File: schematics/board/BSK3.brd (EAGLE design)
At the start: 82 x 100 mm, 44 parts

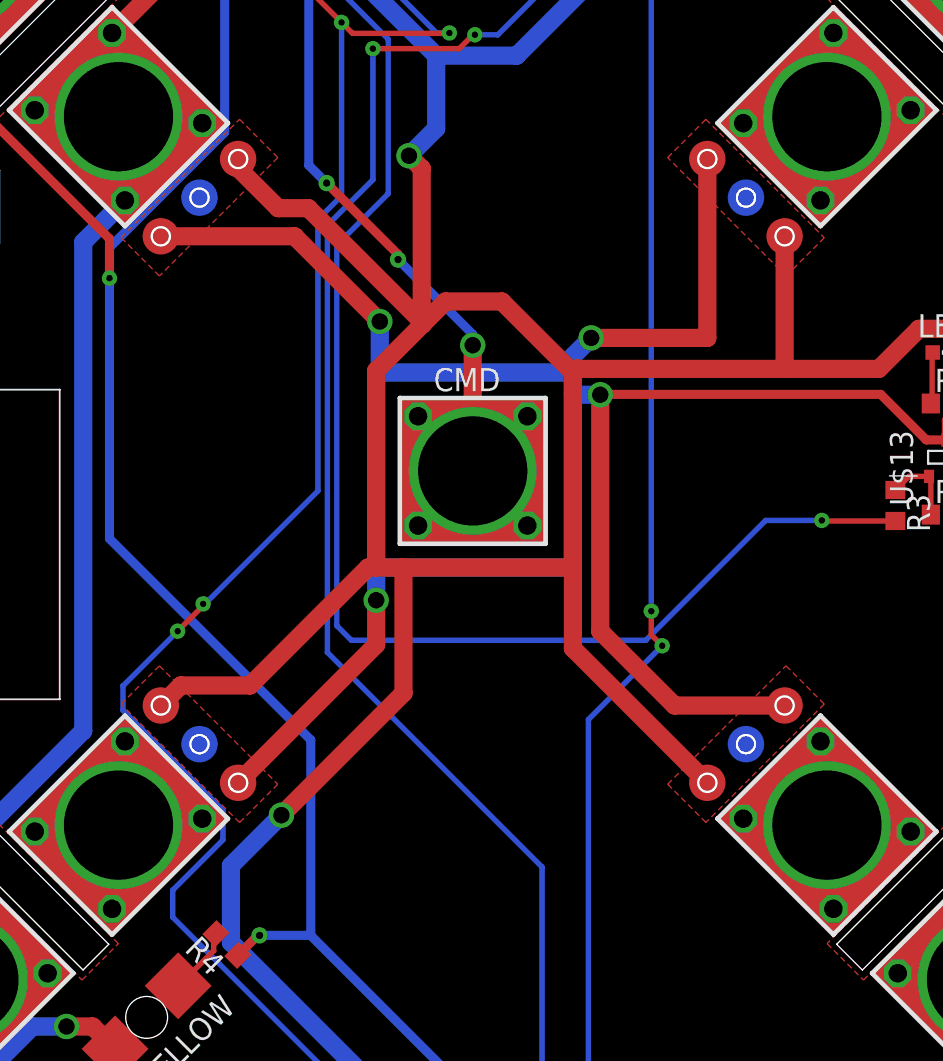
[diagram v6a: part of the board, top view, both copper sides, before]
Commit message: Изменены площадки для сплавов Розе
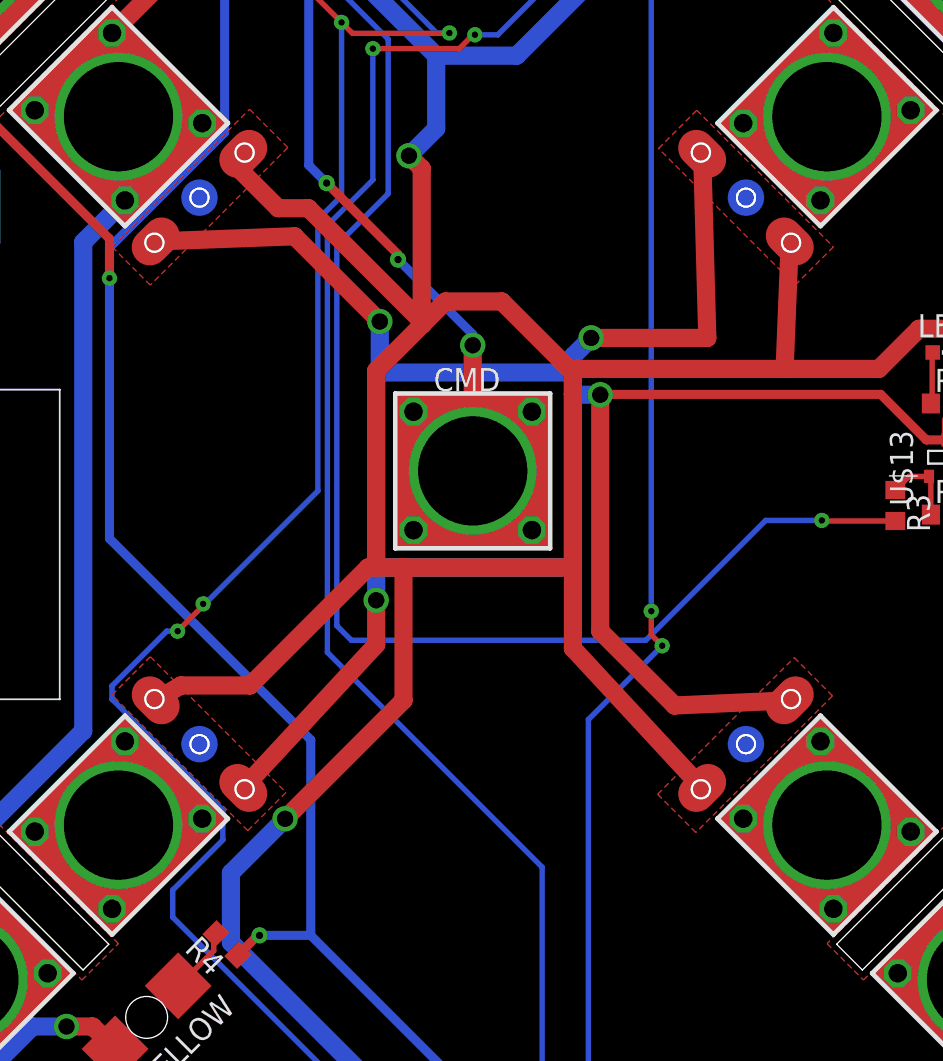
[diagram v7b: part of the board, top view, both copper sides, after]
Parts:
- U$15, U$16, U$6, U$7: value GRAFITGRAFIT3_1 -> GRAFITGRAFIT4_2; device CanCubeSat:GRAFIT3_1 -> CanCubeSat:GRAFIT4_2
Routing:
- net B3-CMD: track 77.6 -> 79.0 mm
- net 2: track 142.1 -> 142.9 mm
- net 1W: track 126.7 -> 127.5 mm
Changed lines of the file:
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@@
 <attribute name="VALUE" x="66.365" y="45.695" size="1.27" layer="27"/>
 </element>
-<element name="U$6" library="CanCubeSat" package="GRAFIT3_1" value="GRAFITGRAFIT3_1" x="26" y="65" smashed="yes" rot="R135"/>
-<element name="U$7" library="CanCubeSat" package="GRAFIT3_1" value="GRAFITGRAFIT3_1" x="26" y="35" smashed="yes" rot="R225"/>
-<element name="U$15" library="CanCubeSat" package="GRAFIT3_1" value="GRAFITGRAFIT3_1" x="56" y="65" smashed="yes" rot="R45"/>
-<element name="U$16" library="CanCubeSat" package="GRAFIT3_1" value="GRAFITGRAFIT3_1" x="56" y="35" smashed="yes" rot="R315"/>
+<element name="U$6" library="CanCubeSat" package="GRAFIT4_2" value="GRAFITGRAFIT4_2" x="26" y="65" smashed="yes" rot="R135"/>
+<element name="U$7" library="CanCubeSat" package="GRAFIT4_2" value="GRAFITGRAFIT4_2" x="26" y="35" smashed="yes" rot="R225"/>
+<element name="U$15" library="CanCubeSat" package="GRAFIT4_2" value="GRAFITGRAFIT4_2" x="56" y="65" smashed="yes" rot="R45"/>
+<element name="U$16" library="CanCubeSat" package="GRAFIT4_2" value="GRAFITGRAFIT4_2" x="56" y="35" smashed="yes" rot="R315"/>
 <element name="R75" library="rcl" library_urn="urn:adsk.eagle:library:334" package="R2512" package3d_urn="urn:adsk.eagle:package:23545/2" value="R01" x="57.1" y="81.2" smashed="yes" rot="R180">
 <attribute name="NAME" x="59.64" y="79.295" size="1.27" layer="25" rot="R180"/>
@@
 <wire x1="24.53" y1="26.98646875" x2="27.283196875" y2="29.739665625" width="0.3" layer="16"/>
 <wire x1="27.283196875" y1="29.739665625" x2="27.283196875" y2="31.377440625" width="0.3" layer="16"/>
-<wire x1="27.283196875" y1="31.377440625" x2="21.8" y2="36.8606375" width="0.3" layer="16"/>
-<wire x1="21.8" y1="36.8606375" x2="21.8" y2="38.2" width="0.3" layer="16"/>
-<wire x1="21.8" y1="38.2" x2="24.8" y2="41.2" width="0.3" layer="16"/>
+<wire x1="27.283196875" y1="31.377440625" x2="21.2" y2="37.4606375" width="0.3" layer="16"/>
+<wire x1="21.2" y1="37.4606375" x2="21.2" y2="38.2" width="0.3" layer="16"/>
+<wire x1="24.2" y1="41.2" x2="21.2" y2="38.2" width="0.3" layer="16"/>
+<wire x1="24.2" y1="41.2" x2="24.8" y2="41.2" width="0.3" layer="16"/>
 <via x="24.8" y="41.2" extent="1-16" drill="0.35"/>
 <wire x1="24.8" y1="41.2" x2="26.2" y2="42.6" width="0.3" layer="1"/>
@@
 <wire x1="35.257359375" y1="44.7" x2="28.778678125" y2="38.22131875" width="1" layer="1"/>
 <wire x1="28.778678125" y1="38.22131875" x2="24.978678125" y2="38.22131875" width="1" layer="1"/>
-<wire x1="24.978678125" y1="38.22131875" x2="23.878678125" y2="37.12131875" width="1" layer="1"/>
+<wire x1="24.978678125" y1="38.22131875" x2="23.595834375" y2="37.4041625" width="1" layer="1"/>
 <wire x1="46.5" y1="55.4" x2="46.5" y2="44.7" width="1" layer="1"/>
 <wire x1="46.5" y1="44.7" x2="37.2" y2="44.7" width="1" layer="1"/>
@@
 <wire x1="67.75" y1="57.05" x2="67" y2="57.8" width="1" layer="1"/>
 <wire x1="67" y1="57.8" x2="65.5" y2="57.8" width="1" layer="1"/>
-<via x="30.5" y="31.1" extent="1-16" drill="0.9"/>
-<wire x1="27.72734375" y1="24.118246875" x2="27.72734375" y2="28.32734375" width="1" layer="16"/>
-<wire x1="27.72734375" y1="28.32734375" x2="30.5" y2="31.1" width="1" layer="16"/>
-<wire x1="30.5" y1="31.1" x2="37.2" y2="37.8" width="1" layer="1"/>
-<wire x1="37.2" y1="37.8" x2="37.2" y2="44.7" width="1" layer="1"/>
+<via x="30.7" y="30.9" extent="1-16" drill="0.9"/>
+<wire x1="27.72734375" y1="24.118246875" x2="27.72734375" y2="27.92734375" width="1" layer="16"/>
+<wire x1="30.7" y1="30.9" x2="27.72734375" y2="27.92734375" width="1" layer="16"/>
+<wire x1="30.7" y1="30.9" x2="37.2" y2="37.4" width="1" layer="1"/>
+<wire x1="37.2" y1="37.4" x2="37.2" y2="44.7" width="1" layer="1"/>
 <wire x1="35.7" y1="55.5" x2="38.2" y2="58" width="1" layer="1"/>
-<wire x1="58.12131875" y1="55.6" x2="58.12131875" y2="62.878678125" width="1" layer="1"/>
-<wire x1="53.878678125" y1="32.878678125" x2="46.5" y2="40.25735625" width="1" layer="1"/>
+<wire x1="58.12131875" y1="55.6" x2="58.4041625" y2="62.595834375" width="1" layer="1"/>
+<wire x1="53.595834375" y1="32.595834375" x2="46.5" y2="40.25735625" width="1" layer="1"/>
 <wire x1="46.5" y1="40.25735625" x2="46.5" y2="44.7" width="1" layer="1"/>
-<wire x1="28.12131875" y1="67.12131875" x2="28.12131875" y2="66.62131875" width="1" layer="1"/>
+<wire x1="28.4041625" y1="67.4041625" x2="28.12131875" y2="66.62131875" width="1" layer="1"/>
 <wire x1="30.32131875" y1="64.42131875" x2="28.12131875" y2="66.62131875" width="1" layer="1"/>
 <wire x1="31.97868125" y1="64.42131875" x2="30.32131875" y2="64.42131875" width="1" layer="1"/>
@@
 <contactref element="U$7" pad="P$1"/>
 <contactref element="U$15" pad="P$1"/>
-<wire x1="28.12131875" y1="32.878678125" x2="35.7" y2="40.457359375" width="1" layer="1"/>
+<wire x1="28.4041625" y1="32.595834375" x2="35.7" y2="40.457359375" width="1" layer="1"/>
 <wire x1="35.7" y1="40.457359375" x2="35.7" y2="42.9" width="1" layer="1"/>
 <via x="35.7" y="42.9" extent="1-16" drill="0.9"/>
@@
 <wire x1="65.9" y1="51.7" x2="67" y2="51.7" width="0.5" layer="1"/>
 <wire x1="63.4" y1="54.2" x2="65.9" y2="51.7" width="0.5" layer="1"/>
-<wire x1="53.878678125" y1="67.12131875" x2="53.878678125" y2="57.3" width="1" layer="1"/>
+<wire x1="53.595834375" y1="67.4041625" x2="53.878678125" y2="57.3" width="1" layer="1"/>
 <wire x1="53.878678125" y1="57.3" x2="47.5" y2="57.3" width="1" layer="1"/>
 <via x="47.5" y="57.3" extent="1-16" drill="0.9"/>
 <wire x1="47.5" y1="57.3" x2="46.5" y2="56.3" width="1" layer="16"/>
 <wire x1="46.5" y1="56.3" x2="46.5" y2="55.4" width="1" layer="16"/>
-<wire x1="58.12131875" y1="37.12131875" x2="52.07868125" y2="37.12131875" width="1" layer="1"/>
+<wire x1="58.4041625" y1="37.4041625" x2="52.07868125" y2="37.12131875" width="1" layer="1"/>
 <wire x1="52.07868125" y1="37.12131875" x2="48" y2="41.2" width="1" layer="1"/>
 <wire x1="48" y1="41.2" x2="48" y2="54.18" width="1" layer="1"/>
@@
 <wire x1="48" y1="54.18" x2="46.52" y2="54.18" width="1" layer="16"/>
 <wire x1="46.52" y1="54.18" x2="46.5" y2="54.2" width="1" layer="16"/>
-<wire x1="23.878678125" y1="62.878678125" x2="31.221321875" y2="62.878678125" width="1" layer="1"/>
+<wire x1="23.595834375" y1="62.595834375" x2="31.221321875" y2="62.878678125" width="1" layer="1"/>
 <wire x1="31.221321875" y1="62.878678125" x2="35.9" y2="58.2" width="1" layer="1"/>
 <via x="35.9" y="58.2" extent="1-16" drill="0.9"/>
@@
 <contactref element="BKU" pad="4"/>
 <wire x1="41.08" y1="49.92" x2="38.22" y2="47.06" width="0.3" layer="1"/>
-<wire x1="38.22" y1="47.06" x2="38" y2="47" width="0.3" layer="1"/>
-<wire x1="41" y1="50" x2="38" y2="53" width="0.3" layer="1"/>
-<wire x1="41.08" y1="49.92" x2="44" y2="47" width="0.3" layer="1"/>
+<wire x1="38.22" y1="47.06" x2="37.75" y2="46.75" width="0.3" layer="1"/>
+<wire x1="41" y1="50" x2="37.75" y2="53.25" width="0.3" layer="1"/>
+<wire x1="41.08" y1="49.92" x2="44.25" y2="46.75" width="0.3" layer="1"/>
 <wire x1="41.08" y1="49.92" x2="43.94" y2="52.78" width="0.3" layer="1"/>
-<wire x1="43.94" y1="52.78" x2="44" y2="53" width="0.3" layer="1"/>
+<wire x1="43.94" y1="52.78" x2="44.25" y2="53.25" width="0.3" layer="1"/>
 <wire x1="41.08" y1="49.92" x2="41" y2="50" width="0.3" layer="1"/>
 <wire x1="41" y1="50" x2="41" y2="56.9" width="1" layer="1"/>
@@
 <signal name="GND3">
 <polygon width="0.15" layer="1" pour="cutout" thermals="no">
-<vertex x="28.2" y="30.7"/>
-<vertex x="21.7" y="37.2"/>
-<vertex x="23.8" y="39.3"/>
-<vertex x="30.3" y="32.8"/>
+<vertex x="28.65" y="30.25"/>
+<vertex x="21.2" y="37.7"/>
+<vertex x="23.3" y="39.8"/>
+<vertex x="30.75" y="32.35"/>
 </polygon>
 </signal>
 <signal name="GND1">
 <polygon width="0.15" layer="1" pour="cutout" thermals="no">
-<vertex x="60.3" y="37.2"/>
-<vertex x="53.8" y="30.7"/>
-<vertex x="51.7" y="32.8"/>
-<vertex x="58.2" y="39.3"/>
+<vertex x="60.75" y="37.65"/>
+<vertex x="53.25" y="30.15"/>
+<vertex x="51.15" y="32.25"/>
+<vertex x="58.65" y="39.75"/>
 </polygon>
 </signal>
 <signal name="GND2">
 <polygon width="0.15" layer="1" pour="cutout" thermals="no">
-<vertex x="58.2" y="60.7"/>
-<vertex x="51.7" y="67.2"/>
-<vertex x="53.8" y="69.3"/>
-<vertex x="60.3" y="62.8"/>
+<vertex x="58.7" y="60.2"/>
+<vertex x="51.2" y="67.7"/>
+<vertex x="53.3" y="69.8"/>
+<vertex x="60.8" y="62.3"/>
 </polygon>
 </signal>
 <signal name="GND4">
 <polygon width="0.15" layer="1" pour="cutout" thermals="no">
-<vertex x="30.3" y="67.2"/>
-<vertex x="23.8" y="60.7"/>
-<vertex x="21.7" y="62.8"/>
-<vertex x="28.2" y="69.3"/>
+<vertex x="30.85" y="67.75"/>
+<vertex x="23.3" y="60.2"/>
+<vertex x="21.2" y="62.3"/>
+<vertex x="28.75" y="69.85"/>
 </polygon>
 </signal>

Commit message: Добавлены подписи Концерна к платам
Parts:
- added U$9: PCB "BSK3", CanCubeSat:ITS-LOGO
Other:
- board text removed: "BSK3 "Концерн ИТС""
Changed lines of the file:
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@@
 <drawing>
 <settings>
-<setting alwaysvectorfont="no"/>
+<setting alwaysvectorfont="yes"/>
 <setting verticaltext="up"/>
 </settings>
@@
 <text x="55.4" y="29.3" size="1.4224" layer="26" rot="MR225">BUS-</text>
 <text x="23.2" y="26" size="1.4224" layer="26" rot="MR135">BUS-</text>
-<text x="40.7" y="74.7" size="2" layer="26" rot="MR0" align="top-center">BSK3
-"Концерн ИТС"</text>
 <text x="27" y="96" size="2" layer="26" rot="MR180">to BKU</text>
 <text x="32" y="4" size="2" layer="26" rot="MR180" align="top-left">to BSK5</text>
@@
 <attribute name="VALUE" x="62.295" y="48.735" size="1.27" layer="27" rot="R270"/>
 </element>
+<element name="U$9" library="CanCubeSat" package="ITS-LOGO" value="PCB &quot;BSK3&quot;" x="57.2" y="9.1" smashed="yes" rot="MR0">
+<attribute name="VALUE" x="57.2" y="7.6" size="1" layer="22" font="vector" ratio="15" rot="MR0"/>
+</element>
 </elements>
 <signals>
@@
 </drawing>
 <compatibility>
-<note version="6.3" minversion="6.2.2" severity="warning">
-Since Version 6.2.2 text objects can contain more than one line,
-which will not be processed correctly with this version.
-</note>
 <note version="8.2" severity="warning">
 Since Version 8.2, EAGLE supports online libraries. The ids
